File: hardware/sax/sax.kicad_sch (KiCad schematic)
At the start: 37 parts, among them J101 Cortex_Debug, J102 JAE_DX07S016JA3, SW101 SW_Push, SW102 SW_Push, U101 TPS78433QWDRBRQ1, U102 ATSAMD51J, Y101 32k768

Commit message: Update library
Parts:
- C101: footprint Capacitor_SMD:C_0603_1608Metric -> V2_Capacitor_SMD:C_0603; symbol Device:C_Small -> V2_Device:C_0603_10u; Manufacturer (none) -> TDK; Mouser (none) -> 810-C1608X6S1A106M; Product (none) -> C1608X6S1A106M080AC
- C102, C103, C104, C105, C106, C111: footprint Capacitor_SMD:C_0603_1608Metric -> V2_Capacitor_SMD:C_0603; symbol Device:C_Small -> V2_Device:C_0603_0u1; Manufacturer (none) -> TDK; Mouser (none) -> 810-CGA3E2X7R1H104MA; Product (none) -> CGA3E2X7R1H104M080AA
- C107, C110: footprint Capacitor_SMD:C_0603_1608Metric -> V2_Capacitor_SMD:C_0603; symbol Device:C_Small -> V2_Device:C_0603_18p; Manufacturer (none) -> YAGEO; Mouser (none) -> 603-CC603JRNPO9BN180; Product (none) -> CC0603JRNPO9BN180
- C108, C109: footprint Capacitor_SMD:C_0805_2012Metric -> V2_Capacitor_SMD:C_0805; symbol Device:C_Small -> V2_Device:C_0805_10u; Manufacturer (none) -> TDK; Mouser (none) -> 810-C2012X5R1E106K; Product (none) -> C2012X5R1E106K125AB; Rating (none) -> 25V
- D101, D102: LCSC (none) -> C965555; Manufacturer (none) -> Worldsemi; Product (none) -> WS2812B-2020
- D103: footprint LED_SMD:LED_0603_1608Metric -> V2_LED:LED_0603; symbol Device:LED_Small -> V2_Device:LED_0603_Orange; Manufacturer (none) -> ROHM Semiconductor; Mouser (none) -> 755-SML-D12M8WT86C; Product (none) -> SML-D12M8WT86C
- D104, D105, D106: value PMEG3010ER -> PMEG6030AEXEX; footprint V2_Diode_SMD:Nexperia_CFP3_SOD-123W -> V2_Diode_SMD:D_SOD-123HP; symbol V2_Diode:PMEG3010ER -> V2_Diode:PMEG6030AEXEX; Manufacturer (none) -> Nexperia; Mouser (none) -> 771-PMEG6030AEXEX; Product (none) -> PMEG6030AEXEX
- ESD101: Manufacturer (none) -> Semtech; Mouser (none) -> 947-RCLAMP0582N.TCT; Product (none) -> RCLAMP0582N.TCT
- FID101, FID102, FID103: value Fiducial -> Fiducial_Paste
- ICON101: footprint V2_Artwork:Logo_Tiny -> V2_Artwork:Logo_Small
- J102: value JAE_DX07S016JA3 -> DX07S016JA3; Manufacturer (none) -> JAE Electronics; Mouser (none) -> 656-DX07S016JA3R1500; Product (none) -> DX07S016JA3R1500
- R101: footprint Resistor_SMD:R_0603_1608Metric -> V2_Resistor_SMD:R_0603; symbol Device:R_Small -> V2_Device:R_0603_330R; Manufacturer (none) -> Vishay; Mouser (none) -> 71-CRCW0603330RFKEAC; Product (none) -> CRCW0603330RFKEAC; Rating (none) -> 100mW
- R102, R103: footprint Resistor_SMD:R_0603_1608Metric -> V2_Resistor_SMD:R_0603; symbol Device:R_Small -> V2_Device:R_0603_5k1; Manufacturer (none) -> Vishay; Mouser (none) -> 71-CRCW06035K10FKEAC; Product (none) -> CRCW06035K10FKEAC; Rating (none) -> 100mW
- R104: footprint Resistor_SMD:R_0603_1608Metric -> V2_Resistor_SMD:R_0603; symbol Device:R_Small -> V2_Device:R_0603_100k; Manufacturer (none) -> Vishay; Mouser (none) -> 71-CRCW0603100KFKEAC; Product (none) -> CRCW0603100KFKEAC; Rating (none) -> 100mW
- SW101, SW102: value SW_Push -> SKSG; symbol Switch:SW_Push -> V2_Switch:SKSG; Manufacturer (none) -> Alps Alpine; Mouser (none) -> 688-SKSGACE010; Product (none) -> SKSGACE010
- TVS101: renamed from TVS102; value SMAJ36CA -> SMBJ36CA; footprint Diode_SMD:D_SMA -> V2_Diode_SMD:D_SMB; symbol V2_Diode:SMAJ36CA -> V2_Diode:SMBJ36CA; Manufacturer (none) -> Bourns; Mouser (none) -> 652-SMBJ36CA-Q; Product (none) -> SMBJ36CA-Q; Rating (none) -> 36V
- U101: Manufacturer (none) -> Texas Instruments; Mouser (none) -> 595-TPS78433QWDRBRQ1; Product (none) -> TPS78433QWDRBRQ1
- U102: Manufacturer (none) -> Microchip Technology; Mouser (none) -> 556-ATSAMD51J19AMU; Product (none) -> ATSAMD51J19A-MU
- Y101: symbol Device:Crystal_Small -> V2_Device:Crystal_3.2x1.5_32k768; Manufacturer (none) -> ABRACON; Mouser (none) -> 815-ABS0716632.768KT; Product (none) -> ABS07-166-32.768KHZ-T
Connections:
- net USB-Shield renamed Shield

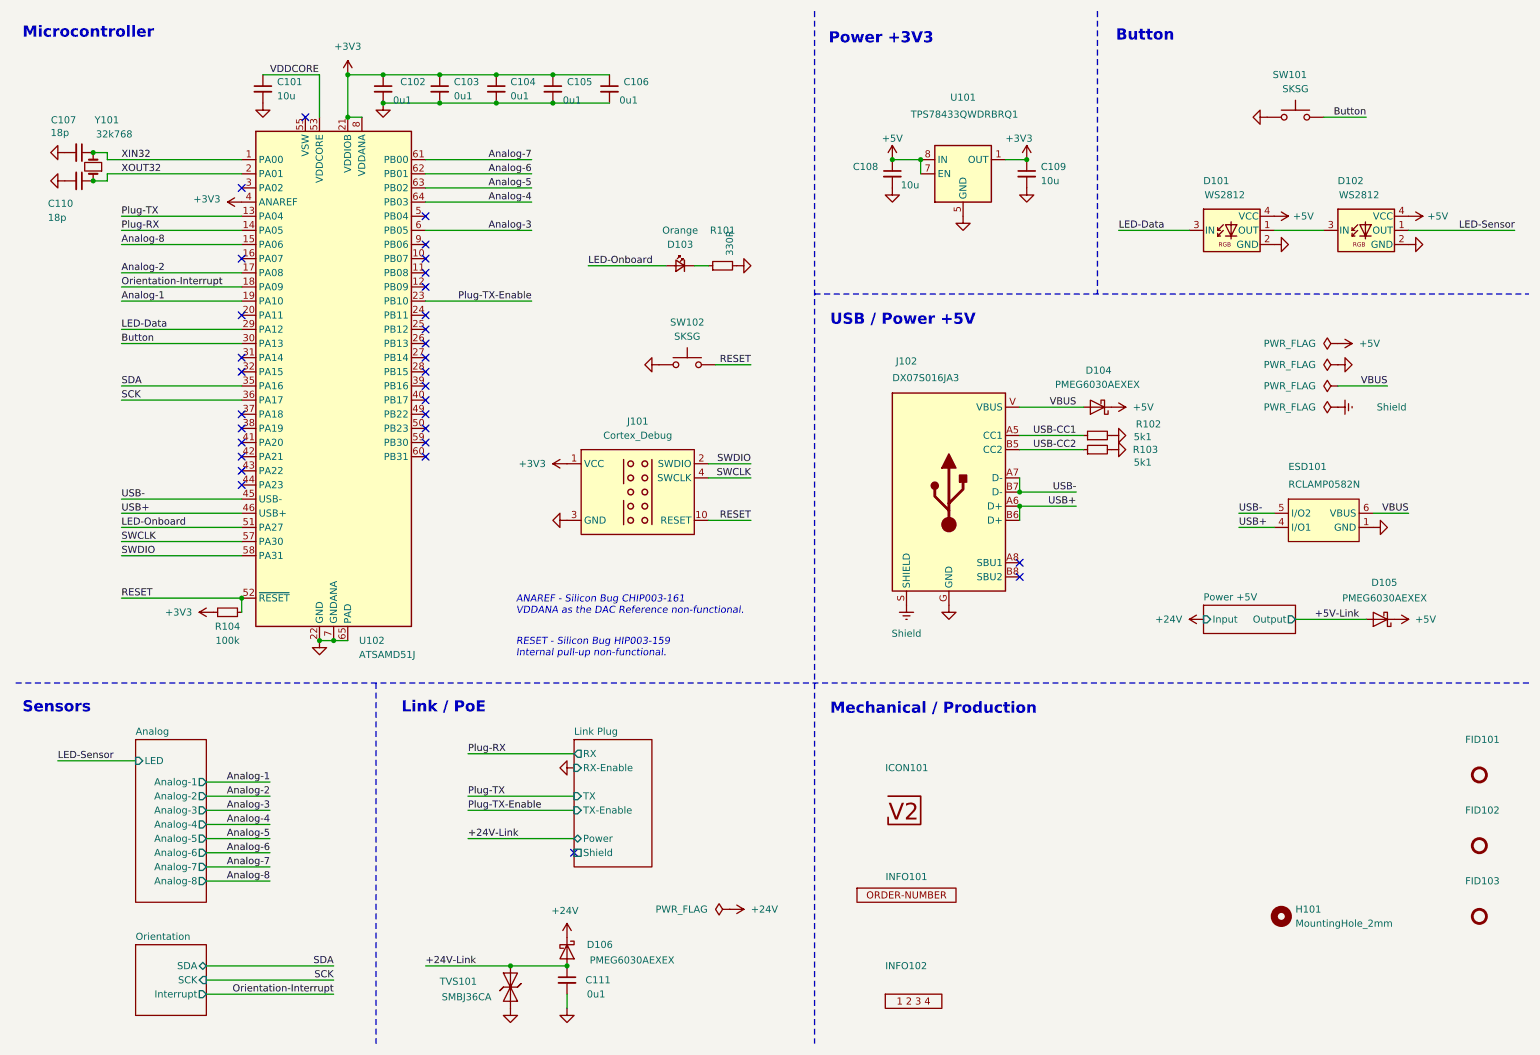
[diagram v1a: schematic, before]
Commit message: Replace Order_Number
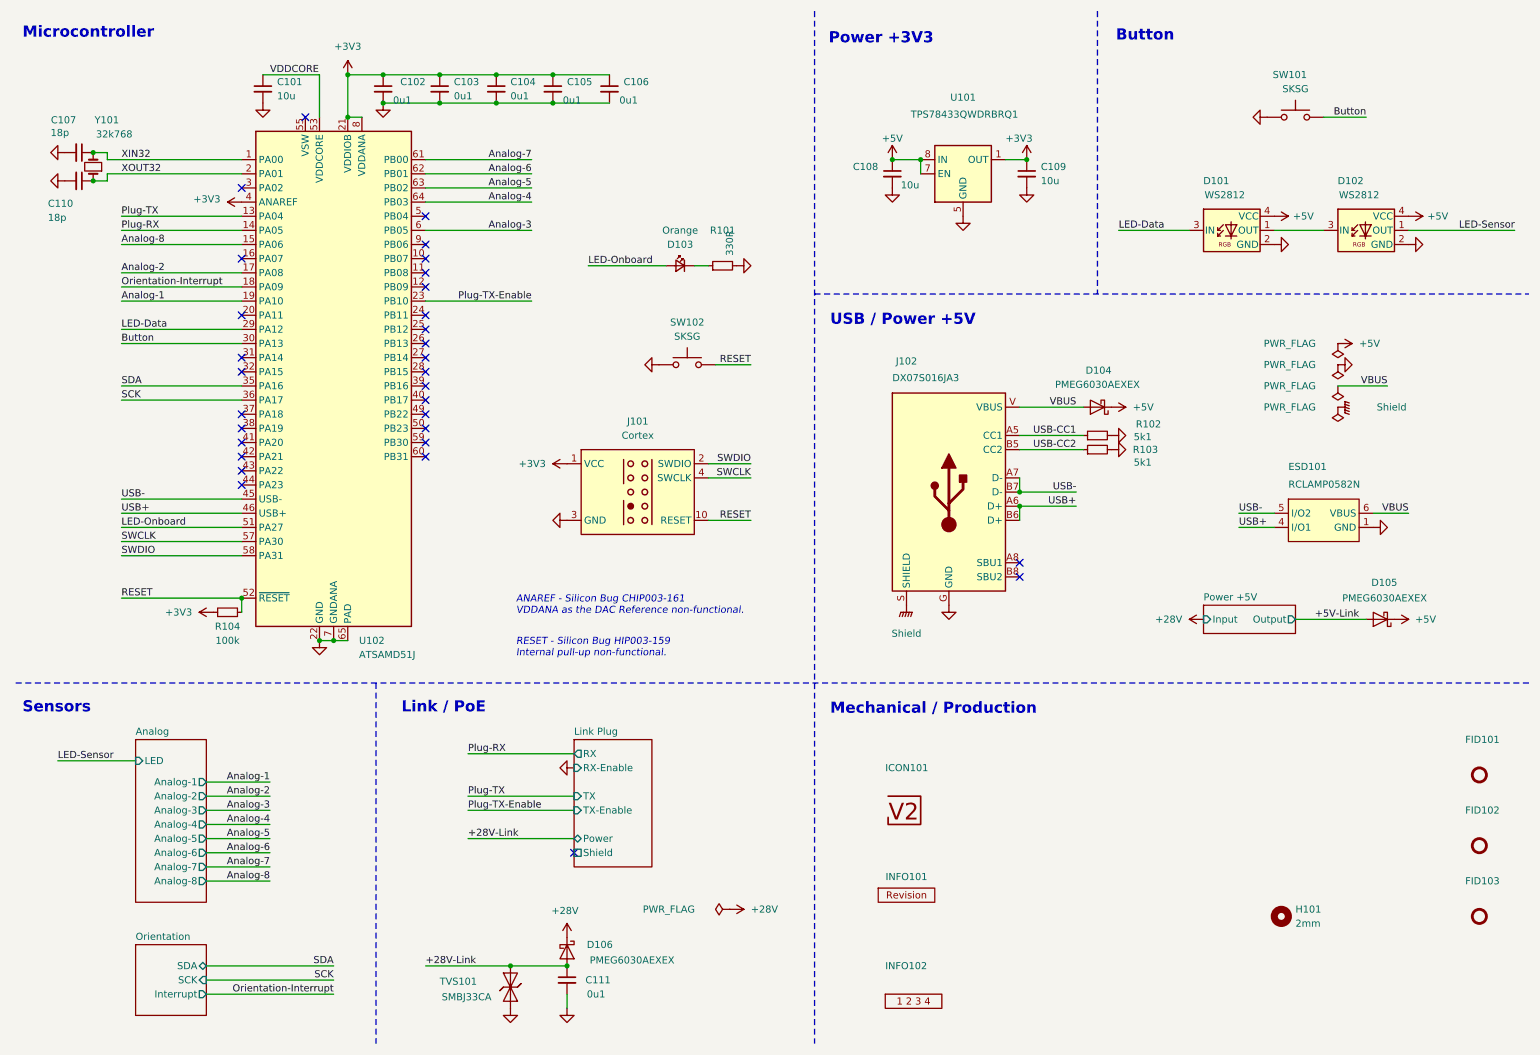
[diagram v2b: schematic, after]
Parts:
- C101: Rating (none) -> 10V
- C102, C103, C104, C105, C106, C111: Rating (none) -> 50V
- D103: Mouser 755-SML-D12M8WT86C -> 755-SML-D12D1WT86; Product SML-D12M8WT86C -> SML-D12D1WT86
- H101: value MountingHole_2mm -> 2mm
- INFO101: value Order_Number -> ~; footprint V2_Production:Order_Number -> V2_Production:Revision; symbol V2_Production:Order_Number -> V2_Production:Revision
- J101: value Cortex_Debug -> Cortex; footprint V2_Cortex_Debug:Cortex_Debug_Pad -> V2_Connector_Debug:Cortex; symbol V2_Cortex_Debug:Cortex_Debug -> V2_Connector_Debug:Cortex
- TVS101: value SMBJ36CA -> SMBJ33CA; symbol V2_Diode:SMBJ36CA -> V2_Diode:SMBJ33CA; Mouser 652-SMBJ36CA-Q -> 652-SMBJ33CA-Q; Product SMBJ36CA-Q -> SMBJ33CA-Q; Rating 36V -> 33V
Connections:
- net +24V renamed +28V
- net +24V-Link renamed +28V-Link

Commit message: Update Library
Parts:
- C101: symbol V2_Device:C_0603_10u -> V2_Capacitor:0603_10u
- C102, C103, C104, C105, C106, C111: symbol V2_Device:C_0603_0u1 -> V2_Capacitor:0603_0u1
- C107, C110: symbol V2_Device:C_0603_18p -> V2_Capacitor:0603_18p
- C108, C109: symbol V2_Device:C_0805_10u -> V2_Capacitor:0805_10u
- D103: symbol V2_Device:LED_0603_Orange -> V2_LED:0603_Orange
- R101: symbol V2_Device:R_0603_330R -> V2_Resistor:0603_330R
- R102, R103: symbol V2_Device:R_0603_5k1 -> V2_Resistor:0603_5k1
- R104: symbol V2_Device:R_0603_100k -> V2_Resistor:0603_100k
- Y101: symbol V2_Device:Crystal_3.2x1.5_32k768 -> V2_Crystal:3.2x1.5_32k768

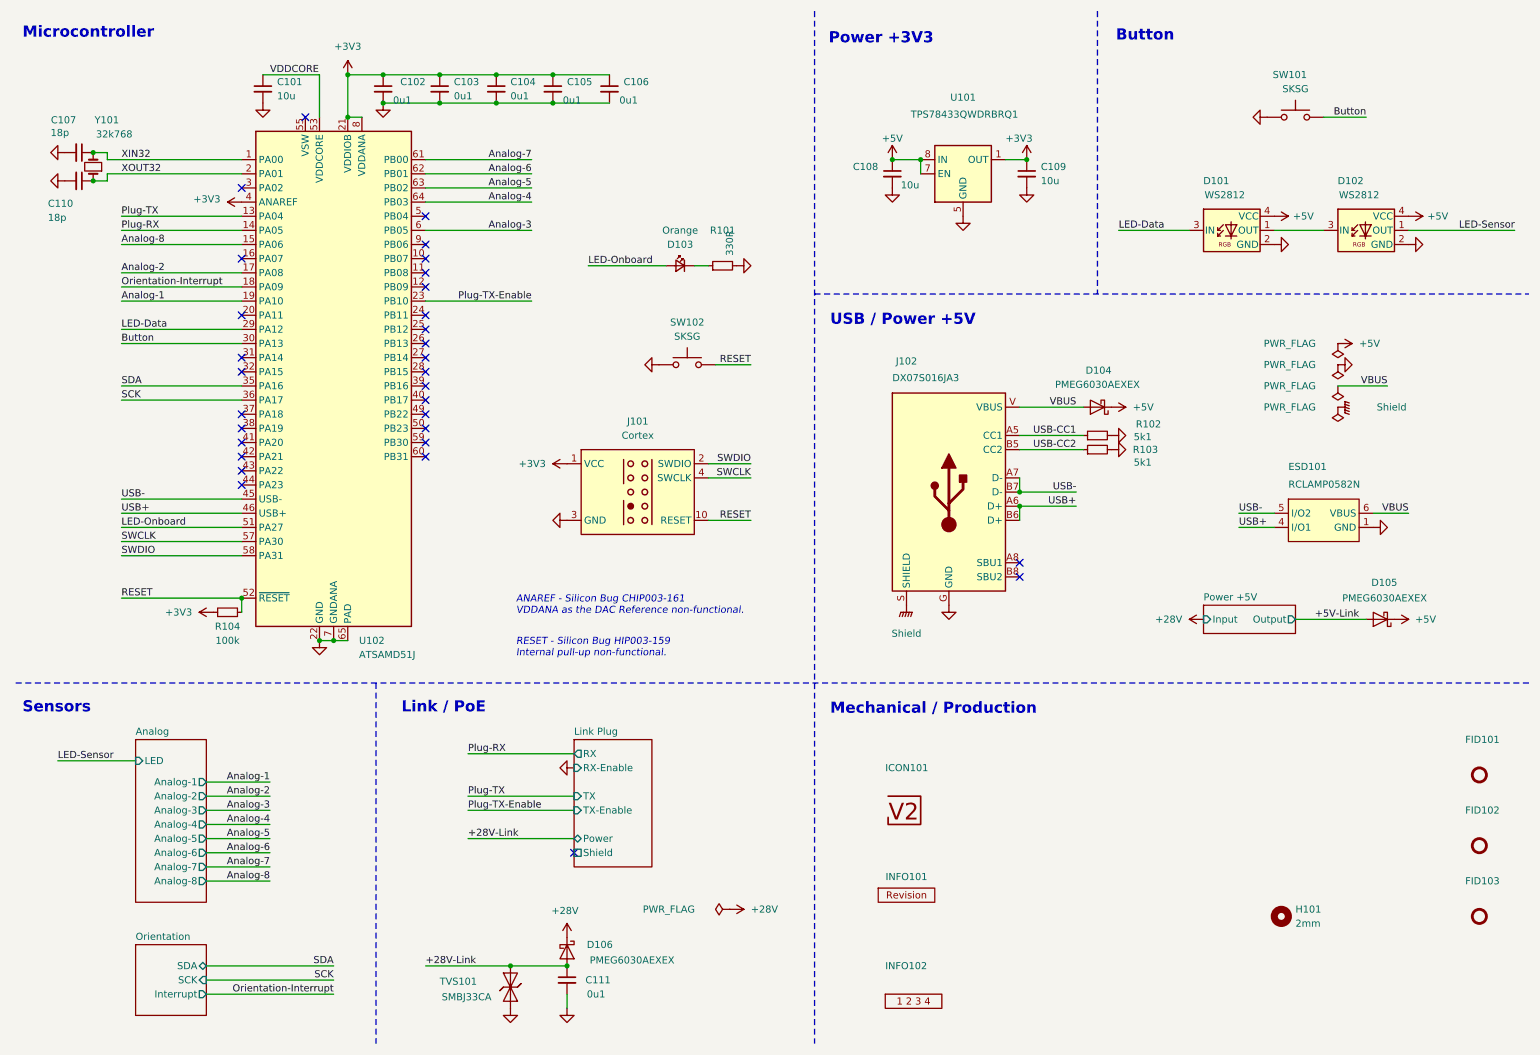
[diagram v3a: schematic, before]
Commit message: sax2 -> sax
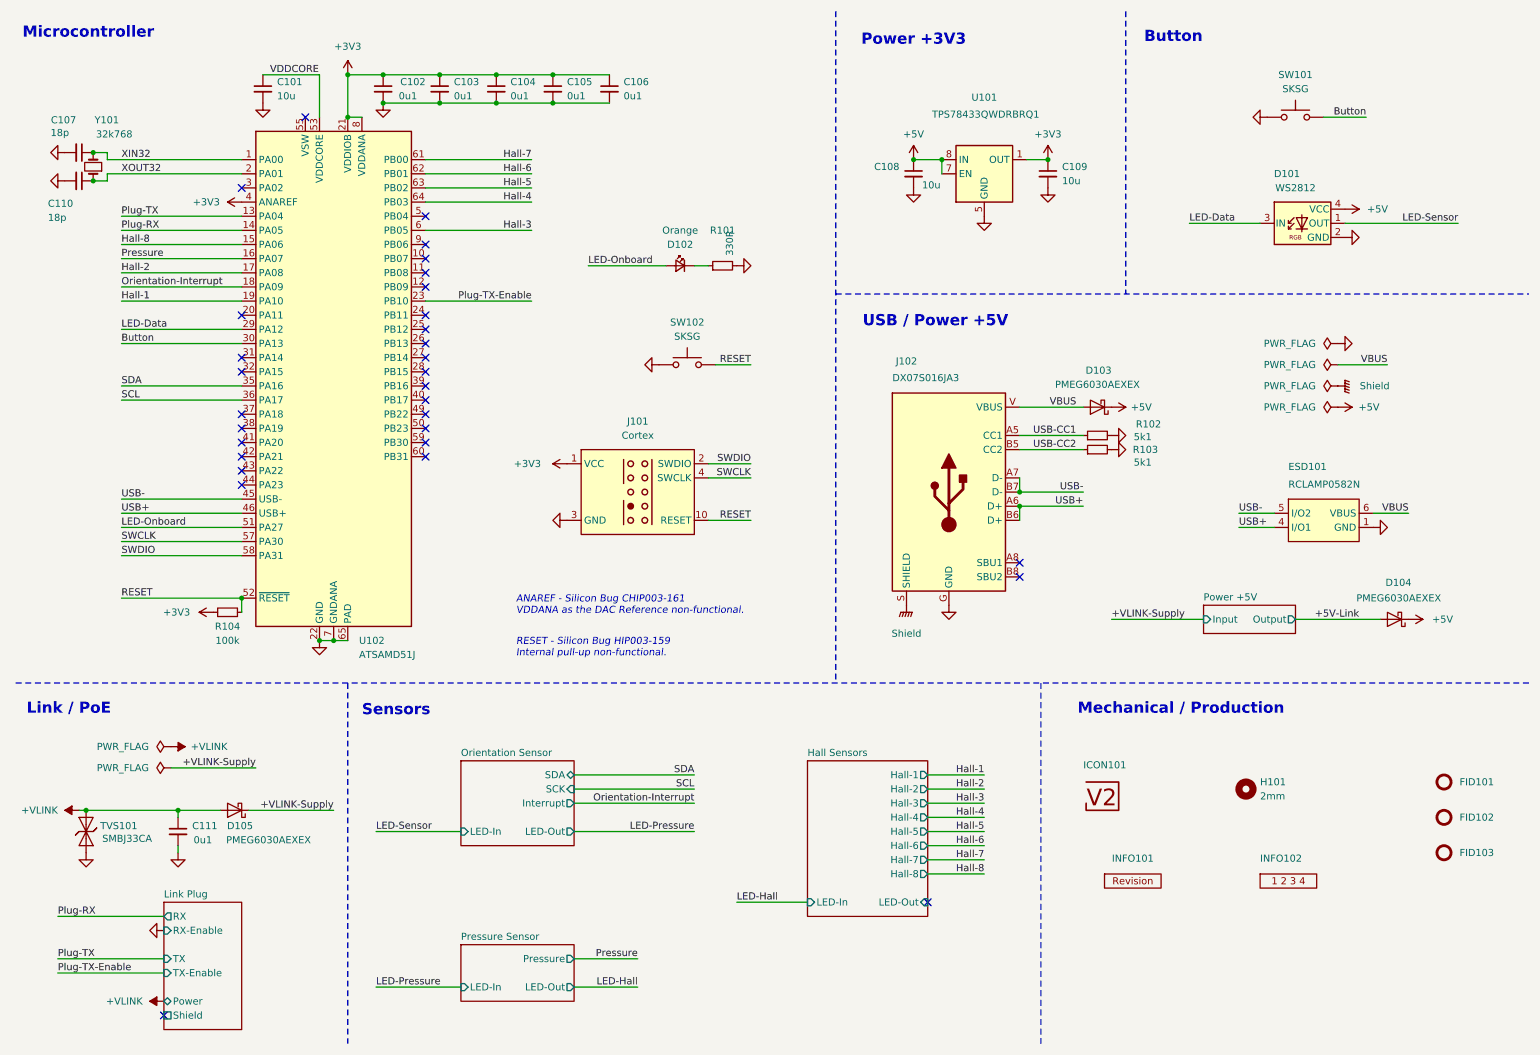
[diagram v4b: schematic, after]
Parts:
- removed D101: WS2812, V2_LED:WS2812-2020, symbol V2_LED:WS2812
- renumbered D102 to D101, D103 to D102, D104 to D103, D105 to D104, D106 to D105
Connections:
- net LED-Data: now also D101.3 (IN)
- net Pressure: now reaches U102.16 (PA07)
- net +28V renamed +VLINK-Supply
- net +28V-Link renamed +VLINK
- net Analog-1 renamed Hall-1
- net Analog-2 renamed Hall-2
- net Analog-3 renamed Hall-3
- net Analog-4 renamed Hall-4
- net Analog-5 renamed Hall-5
- net Analog-6 renamed Hall-6
- net Analog-7 renamed Hall-7
- net Analog-8 renamed Hall-8
- net SCK renamed SCL
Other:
- sheet Analog renamed Hall Sensors
- sheet Orientation renamed Orientation Sensor
- added sheet Pressure Sensor (PressureSensor.kicad_sch)
- sheet Hall Sensors: file AnalogSensors.kicad_sch -> HallSensors.kicad_sch
- sheet Hall Sensors ports: added Hall-1, Hall-2, Hall-3, Hall-4, Hall-5, Hall-6, Hall-7, Hall-8, LED-In, LED-Out; removed Analog-1, Analog-2, Analog-3, Analog-4, Analog-5, Analog-6, Analog-7, Analog-8, LED
- sheet Orientation Sensor ports: added LED-In, LED-Out; removed none
- note added: "ANAREF - Silicon Bug CHIP003-161 VDDANA as the DAC Reference non-functional."
- note added: "RESET - Silicon Bug HIP003-159 Internal pull-up non-functional."
- note removed: "ANAREF - ﻿Silicon Bug CHIP003-161 VDDANA as the DAC Reference non-functional."
- note removed: "RESET - ﻿Silicon Bug HIP003-159 Internal pull-up non-functional."
- moved on the sheet: C108, C109, C111, D101, D104, D105, FID101, FID102, FID103, H101, ICON101, INFO101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

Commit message: Refresh
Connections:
- net VBUS renamed +VBUS
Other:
- moved on the sheet: C108, C109, D101, D103, D104, ESD101, SW101, U101

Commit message: Export stencil
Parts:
- INFO101: value ~ -> (none)
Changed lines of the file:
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@@
 	(title_block
 		(title "V2 sax")
-		(date "2026-02-18")
+		(date "2026-02-25")
 		(rev "2026-02-10")
 		(company "Versio Duo")
@@
 		(dnp no)
 		(fields_autoplaced yes)
-		(property "Reference" "#PWR0138"
+		(property "Reference" "#PWR138"
 			(at 215.9 64.77 0)
 			(effects
@@
 			(project "sax"
 				(path "/6c8448b4-b04d-47e1-934e-e40cbe27a7be"
-					(reference "#PWR0138")
+					(reference "#PWR138")
 					(unit 1)
 				)
@@
 			)
 		)
-		(property "Value" "~"
+		(property "Value" ""
 			(at 213.36 171.45 0)
 			(effects
@@
 		(dnp no)
 		(fields_autoplaced yes)
-		(property "Reference" "#PWR0137"
+		(property "Reference" "#PWR137"
 			(at 180.34 83.82 0)
 			(effects
@@
 			(project ""
 				(path "/6c8448b4-b04d-47e1-934e-e40cbe27a7be"
-					(reference "#PWR0137")
+					(reference "#PWR137")
 					(unit 1)
 				)
@@
 		(dnp no)
 		(fields_autoplaced yes)
-		(property "Reference" "#PWR0139"
+		(property "Reference" "#PWR139"
 			(at 266.7 109.22 0)
 			(effects
@@
 			(project "sax"
 				(path "/6c8448b4-b04d-47e1-934e-e40cbe27a7be"
-					(reference "#PWR0139")
+					(reference "#PWR139")
 					(unit 1)
 				)
